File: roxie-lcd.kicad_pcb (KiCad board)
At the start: 2 copper layers, 11 parts, among them J1 Arduino-NANO-Every, J2 VESC, J3 TFT, J4 BUTTON 1, J5 BUTTON 2, J6 BUTTON 3, J7 SD

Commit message: Added photos
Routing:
- net GND: track 0.00 -> 13.7 mm
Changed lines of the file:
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@@
     (thickness 1.6)
     (drawings 10)
-    (tracks 94)
+    (tracks 102)
     (zones 0)
     (modules 11)
@@
   )
   (setup
-    (last_trace_width 0.25)
+    (last_trace_width 1)
     (user_trace_width 0.2)
     (user_trace_width 0.3)
@@
   (via (at 85 50) (size 0.8) (drill 0.4) (layers F.Cu B.Cu) (net 26))
   (via (at 42 63) (size 0.8) (drill 0.4) (layers F.Cu B.Cu) (net 26))
+  (segment (start 81.04 55.055) (end 82.695 53.4) (width 1) (layer F.Cu) (net 26))
+  (segment (start 81.04 57.555) (end 81.04 55.055) (width 1) (layer F.Cu) (net 26))
+  (segment (start 84.600001 53.399999) (end 85 53) (width 1) (layer F.Cu) (net 26))
+  (segment (start 82.695 53.4) (end 84.600001 53.399999) (width 1) (layer F.Cu) (net 26))
+  (segment (start 81.04 60.055) (end 80.8 60.295) (width 1) (layer F.Cu) (net 26))
+  (segment (start 81.04 57.555) (end 81.04 60.055) (width 1) (layer F.Cu) (net 26))
+  (segment (start 79.705 60.295) (end 78 62) (width 1) (layer F.Cu) (net 26))
+  (segment (start 80.8 60.295) (end 79.705 60.295) (width 1) (layer F.Cu) (net 26))
   (via (at 46.1 57.5) (size 0.8) (drill 0.4) (layers F.Cu B.Cu) (net 27))
   (segment (start 46.1 57.5) (end 46.1 56.934315) (width 0.5) (layer B.Cu) (net 27))

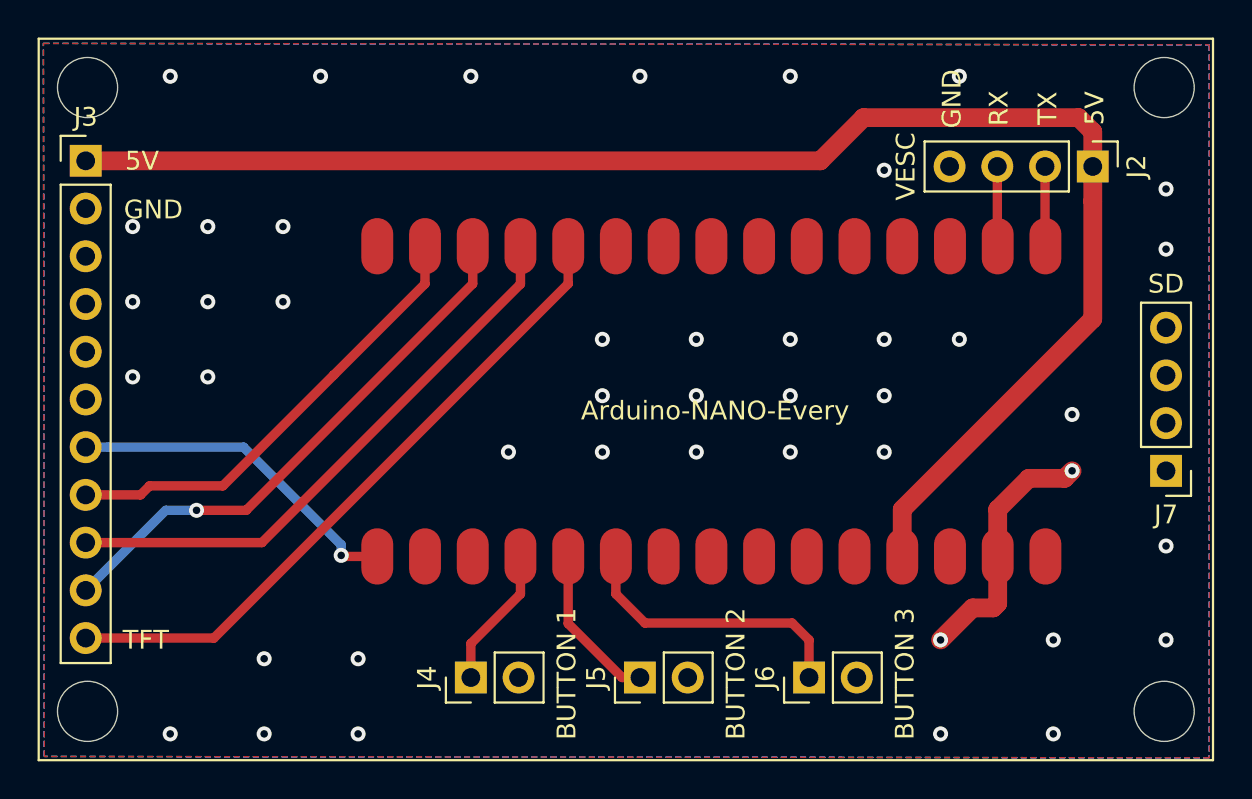
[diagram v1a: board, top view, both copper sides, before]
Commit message: Changed VESC connector to PH and added SD card support
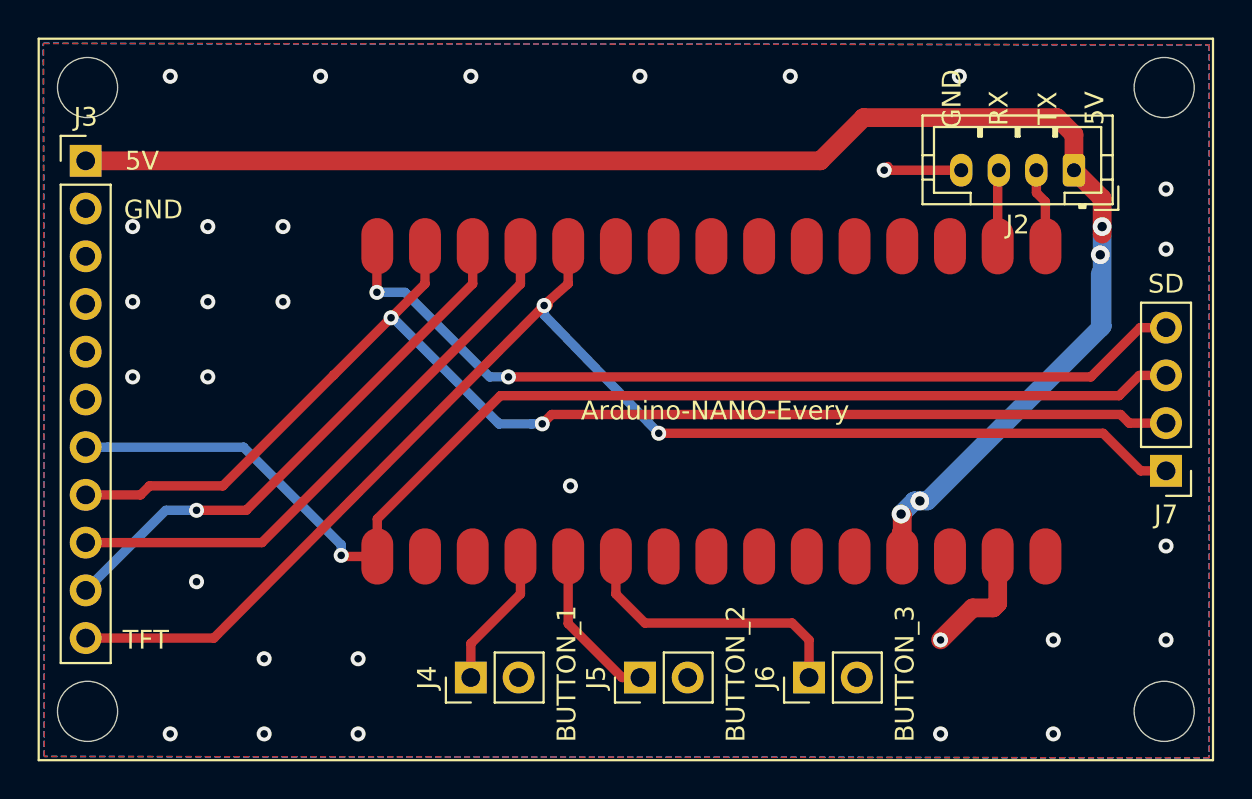
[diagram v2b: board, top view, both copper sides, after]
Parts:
- H2, H4: value M -> MountingHole
- J2: footprint Connector_PinHeader_2.54mm:PinHeader_1x04_P2.54mm_Vertical -> Connector_JST:JST_PH_B4B-PH-K_1x04_P2.00mm_Vertical
- J4: value BUTTON 1 -> BUTTON_1
- J5: value BUTTON 2 -> BUTTON_2
- J6: value BUTTON 3 -> BUTTON_3
- moved J2 1.02 mm to (85.1, 37.0), turned to 180 degrees
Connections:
- J1 pad 30: Net-(J1-Pad30) -> MISO
- J7 pad 1: Net-(J7-Pad1) -> CS
- J7 pad 2: Net-(J7-Pad2) -> SDA
- J7 pad 3: Net-(J7-Pad3) -> CLK
- J7 pad 4: Net-(J7-Pad4) -> MISO
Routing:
- net MISO: track 0.00 -> 47.4 mm, vias 0 -> 2
- net CLK: track 18.3 -> 65.4 mm
- net SDA: track 24.7 -> 68.9 mm, vias 0 -> 2
- net CS: track 35.5 -> 73.0 mm, vias 0 -> 2
- net 5V: track 81.7 -> 88.2 mm, vias 0 -> 4
- net GND: track 13.7 -> 10.7 mm, vias 44 -> 30
- net TX: track 4.25 -> 5.01 mm
